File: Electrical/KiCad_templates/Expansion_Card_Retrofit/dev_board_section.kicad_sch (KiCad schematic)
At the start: 19 parts, among them Q1 DMG1012T, Q2 Q_PMOS_SGD, U2 RP2040, U3 W25Q16JVUXIQ

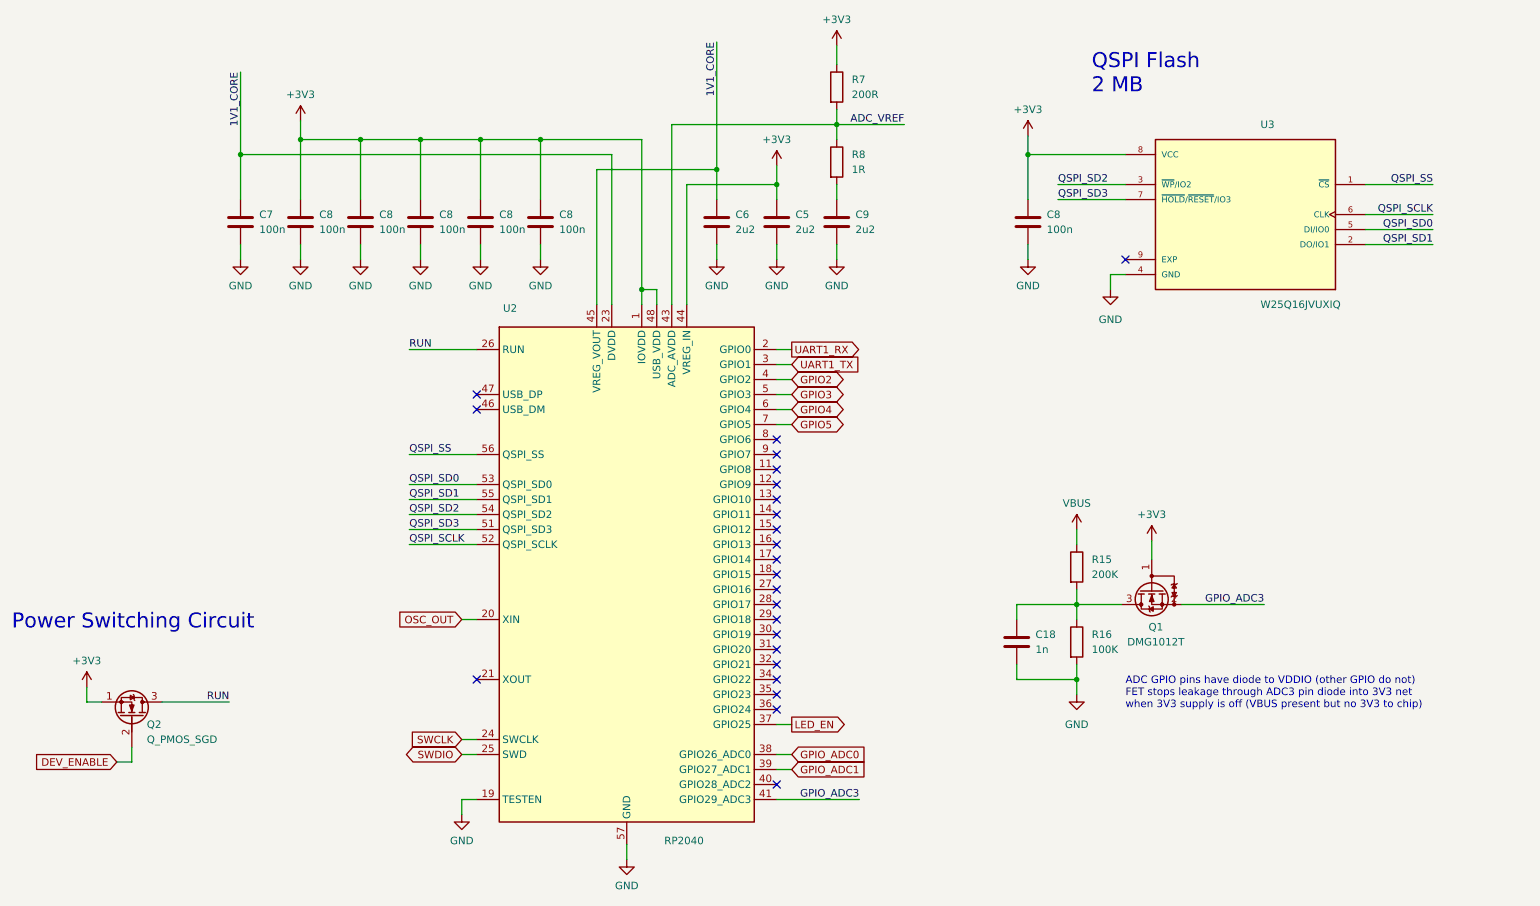
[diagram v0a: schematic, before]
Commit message: Added test points
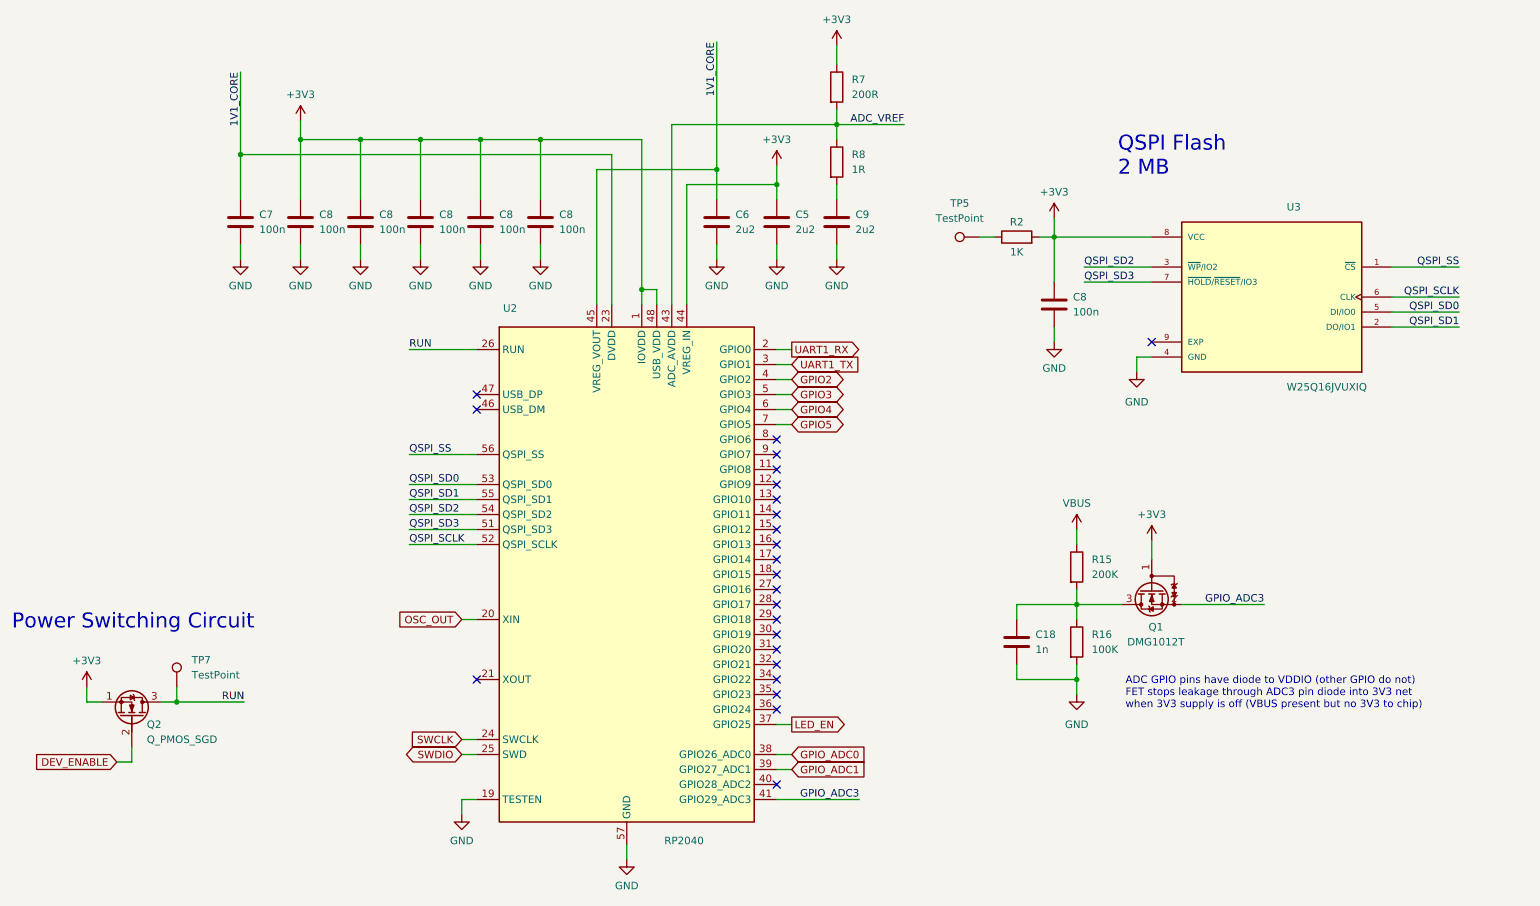
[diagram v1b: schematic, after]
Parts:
- added R2: 1K, Resistor_SMD:R_0402_1005Metric, symbol Device:R
- added TP5, TP7: TestPoint, TestPoint:TestPoint_Pad_1.0x1.0mm, symbol Connector:TestPoint
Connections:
- net +3V3: now also R2.2
- net RUN: now also TP7.1
- new net: R2.1, TP5.1
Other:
- moved on the sheet: C8, U3

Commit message: Production design v1 finished
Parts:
- Q2: footprint Package_DFN_QFN:Diodes_DFN1006-3 -> Package_TO_SOT_SMD:SOT-723
- TP5: value TestPoint -> BOOT
- TP7: value TestPoint -> RST2
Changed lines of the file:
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@@
       (effects (font (size 1.27 1.27)) (justify left))
     )
-    (property "Value" "TestPoint" (at 52.07 139.573 0)
+    (property "Value" "RST2" (at 52.07 139.573 0)
       (effects (font (size 1.27 1.27)) (justify left))
     )
@@
       (effects (font (size 1.27 1.27)))
     )
-    (property "Value" "TestPoint" (at 182.118 62.23 90)
+    (property "Value" "BOOT" (at 182.118 62.23 90)
       (effects (font (size 1.27 1.27)))
     )
@@
       (effects (font (size 1.27 1.27)) (justify left))
     )
-    (property "Footprint" "Package_DFN_QFN:Diodes_DFN1006-3" (at 44.45 141.605 0)
-      (effects (font (size 1.27 1.27)) hide)
-    )
+    (property "Footprint" "Package_TO_SOT_SMD:SOT-723" (at 44.45 141.605 0)
+      (effects (font (size 1.27 1.27)) hide)
+    )
